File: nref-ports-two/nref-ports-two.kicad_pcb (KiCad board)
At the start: 2 copper layers, 88 x 24.9 mm, 6 parts, among them J1 USB_C_Receptacle, J2 USB_C_Receptacle, J3 WURTH_692121230100, J4 HD0919MSMTTR

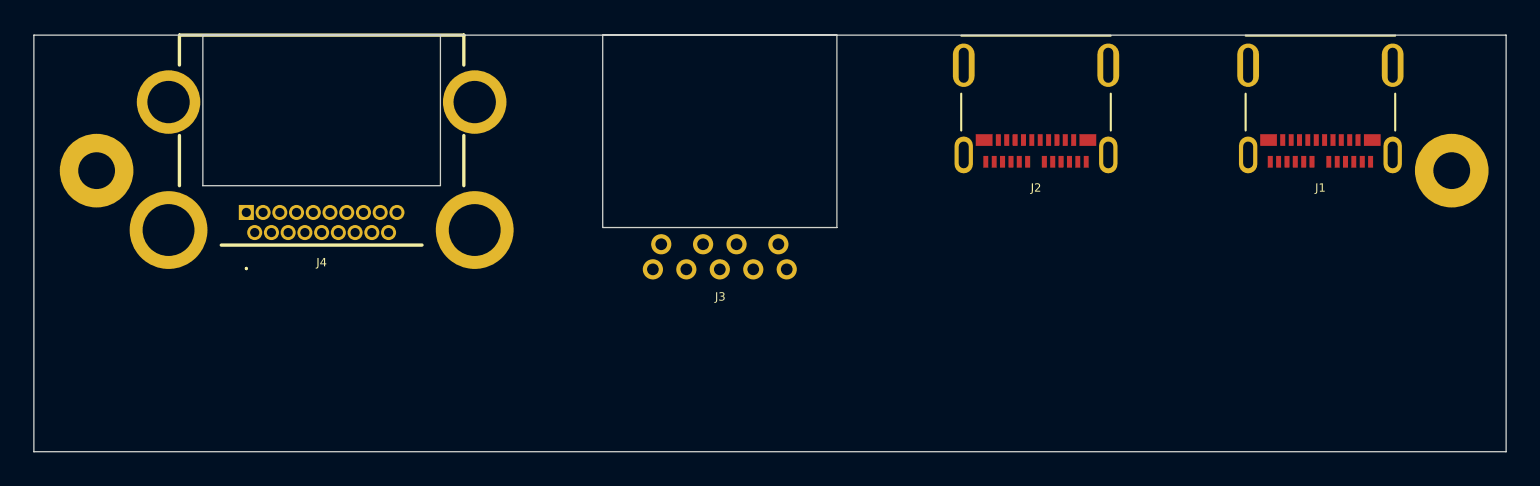
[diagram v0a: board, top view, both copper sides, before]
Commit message: ports 1 routing, ports 2 location tweaks
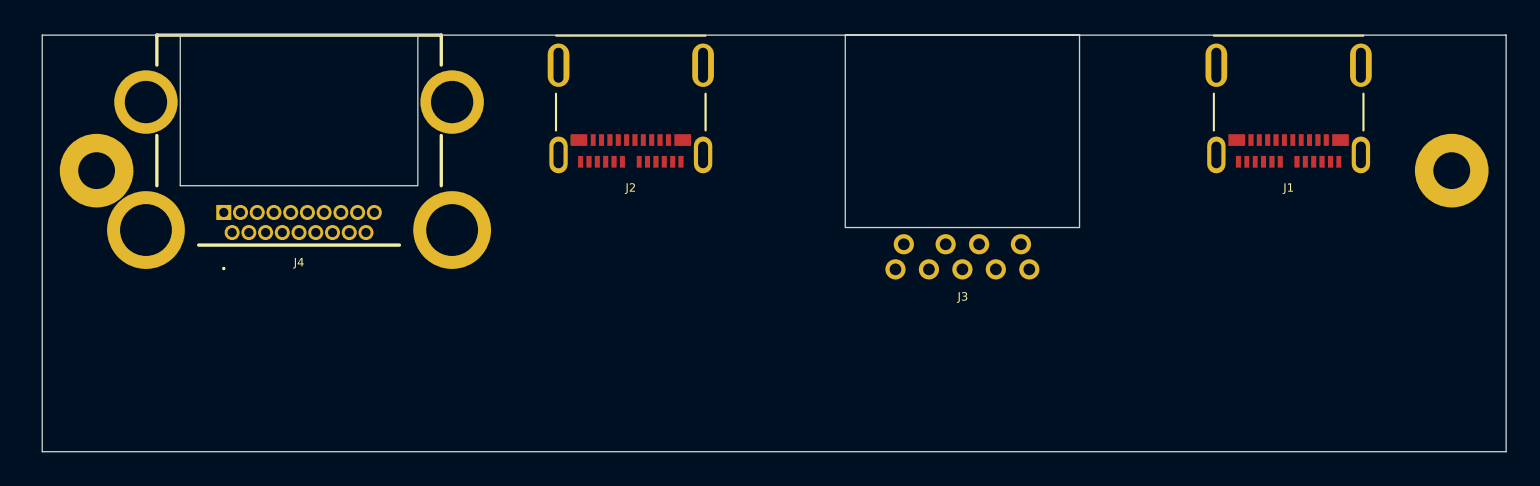
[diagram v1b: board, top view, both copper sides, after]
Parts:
- moved J2 24.2 mm to (135.7, 83.8)
- moved J3 14.5 mm to (155.5, 94.0)
- moved J1 1.90 mm to (175.0, 83.8)
- moved J4 1.35 mm to (111.3, 90.6)
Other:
- board size 88 x 24.9 mm -> 87.5 x 24.9 mm
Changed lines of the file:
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@@
 				(font
 					(size 1.27 1.27)
+					(thickness 0.15)
 				)
 			)
@@
 				(font
 					(size 1.27 1.27)
+					(thickness 0.15)
 				)
 			)
@@
 				(font
 					(size 1.27 1.27)
+					(thickness 0.15)
 				)
 			)
@@
 				(font
 					(size 1.27 1.27)
+					(thickness 0.15)
 				)
 			)
@@
 				(font
 					(size 1.27 1.27)
+					(thickness 0.15)
 				)
 			)
@@
 				(font
 					(size 1.27 1.27)
+					(thickness 0.15)
 				)
 			)
@@
 	(footprint "footprints:HD0919MSMTTR"
 		(layer "F.Cu")
-		(at 112.7 90.6)
+		(at 111.35 90.6)
 		(descr "HD09-19-MSMT-TR-3")
 		(tags "Connector")
@@
 				(font
 					(size 1.27 1.27)
+					(thickness 0.15)
 				)
 			)
@@
 				(font
 					(size 1.27 1.27)
+					(thickness 0.15)
 				)
 			)
@@
 				(font
 					(size 1.27 1.27)
+					(thickness 0.15)
 				)
 			)
@@
 	(footprint "footprints:WURTH_692121230100"
 		(layer "F.Cu")
-		(at 141 94 180)
+		(at 155.5 94 180)
 		(property "Reference" "J3"
 			(at -0.02855 -1.63745 0)
@@
 				(font
 					(size 1.27 1.27)
+					(thickness 0.15)
 				)
 			)
@@
 				(font
 					(size 1.27 1.27)
+					(thickness 0.15)
 				)
 			)
@@
 				(font
 					(size 1.27 1.27)
+					(thickness 0.15)
 				)
 			)
@@
 	(footprint "footprints:MOLEX_105450-0101"
 		(layer "F.Cu")
-		(at 159.9 83.8 180)
+		(at 135.68 83.8 180)
 		(property "Reference" "J2"
 			(at -0.000875 -5.327165 0)
@@
 				(font
 					(size 1.27 1.27)
+					(thickness 0.15)
 				)
 			)
@@
 				(font
 					(size 1.27 1.27)
+					(thickness 0.15)
 				)
 			)
@@
 				(font
 					(size 1.27 1.27)
+					(thickness 0.15)
 				)
 			)
@@
 			(polygon
 				(pts
-					(xy 163.40241 85.68) (xy 156.4 85.68) (xy 156.4 80.0274) (xy 163.40241 80.0274)
+					(xy 139.18241 85.68) (xy 132.18 85.68) (xy 132.18 80.0274) (xy 139.18241 80.0274)
 				)
 			)
@@
 	(footprint "footprints:MOLEX_105450-0101"
 		(layer "F.Cu")
-		(at 176.9 83.8 180)
+		(at 175 83.8 180)
 		(property "Reference" "J1"
 			(at -0.000875 -5.327165 0)
@@
 				(font
 					(size 1.27 1.27)
+					(thickness 0.15)
 				)
 			)
@@
 				(font
 					(size 1.27 1.27)
+					(thickness 0.15)
 				)
 			)
@@
 				(font
 					(size 1.27 1.27)
+					(thickness 0.15)
 				)
 			)
@@
 			(polygon
 				(pts
-					(xy 180.40241 85.68) (xy 173.4 85.68) (xy 173.4 80.0274) (xy 180.40241 80.0274)
+					(xy 178.50241 85.68) (xy 171.5 85.68) (xy 171.5 80.0274) (xy 178.50241 80.0274)
 				)
 			)
@@
 	)
 	(gr_rect
-		(start 100 80)
+		(start 100.5 80)
 		(end 188 104.9)
 		(stroke

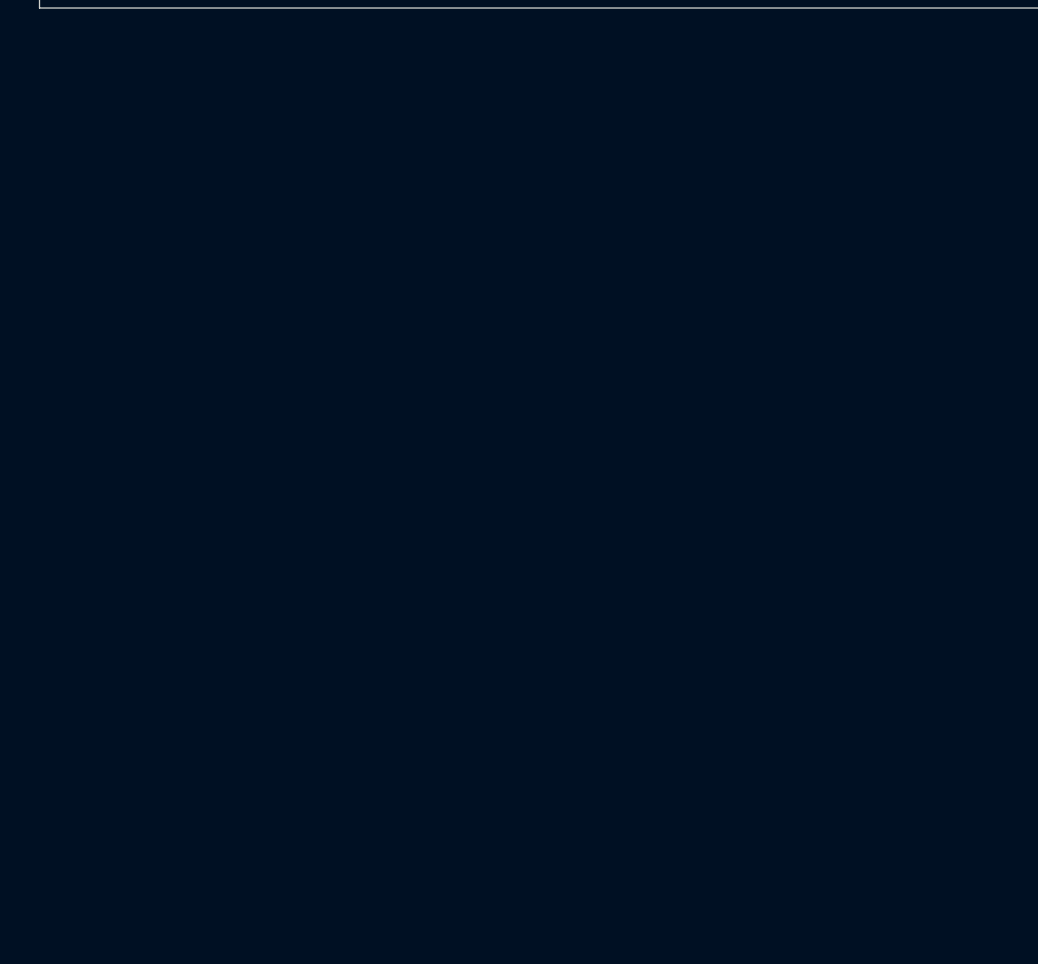
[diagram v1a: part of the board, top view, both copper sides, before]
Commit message: ports two: initial (mostly complete) schematic
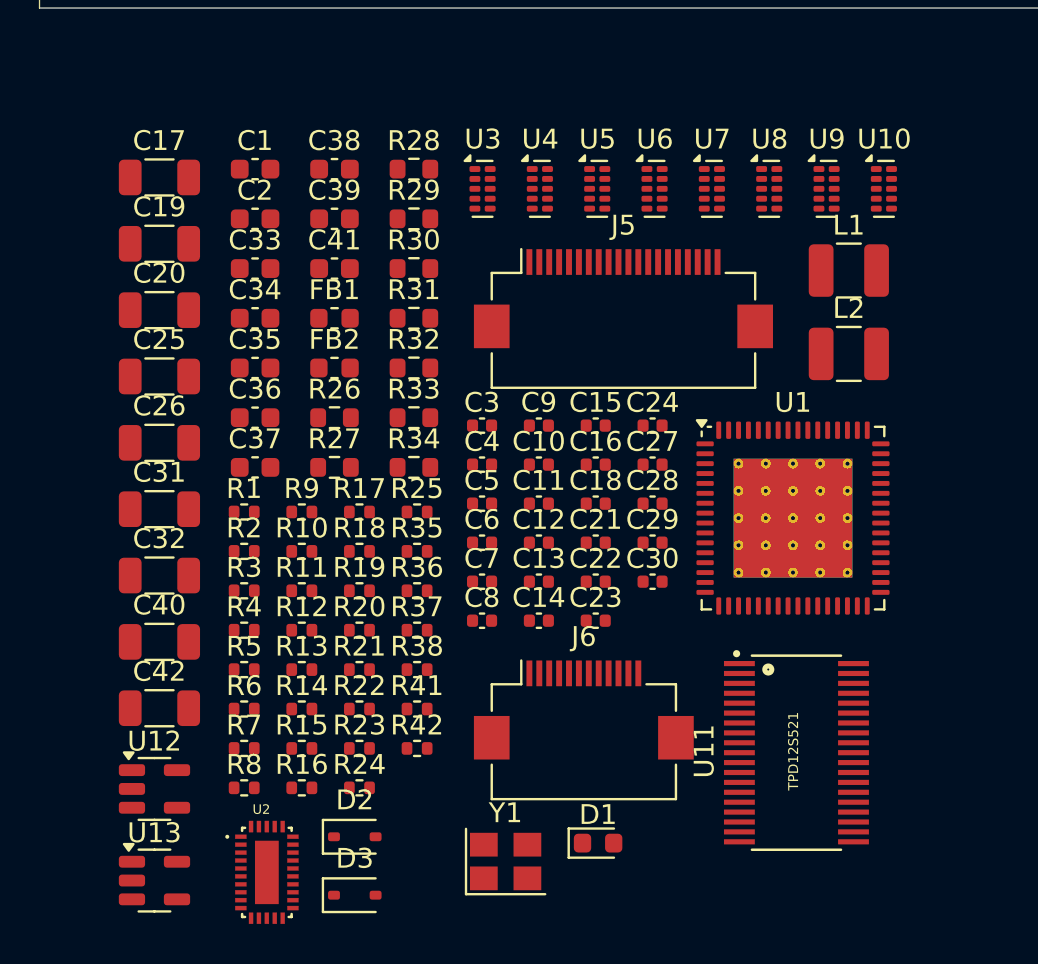
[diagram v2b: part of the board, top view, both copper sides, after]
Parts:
- added C1: 18pF, Capacitor_SMD:C_0603_1608Metric, F.Cu at (111.4, 113.0)
- added C10: 0.1uF, Capacitor_SMD:C_0402_1005Metric, F.Cu at (125.7, 128.0)
- added C11: 0.1uF, Capacitor_SMD:C_0402_1005Metric, F.Cu at (125.7, 129.9)
- added C12: 10uF, Capacitor_SMD:C_0402_1005Metric, F.Cu at (125.7, 131.9)
- added C13: 0.1uF, Capacitor_SMD:C_0402_1005Metric, F.Cu at (125.7, 133.9)
- added C14: 0.1uF, Capacitor_SMD:C_0402_1005Metric, F.Cu at (125.7, 135.8)
- added C15: 0.1uF, Capacitor_SMD:C_0402_1005Metric, F.Cu at (128.6, 126.0)
- added C16: 10uF, Capacitor_SMD:C_0402_1005Metric, F.Cu at (128.6, 128.0)
- added C17: 47uF, Capacitor_SMD:C_1206_3216Metric, F.Cu at (106.6, 113.5)
- added C18: 0.1uF, Capacitor_SMD:C_0402_1005Metric, F.Cu at (128.6, 129.9)
- added C19: 47uF, Capacitor_SMD:C_1206_3216Metric, F.Cu at (106.6, 116.8)
- added C2: 18pF, Capacitor_SMD:C_0603_1608Metric, F.Cu at (111.4, 115.5)
- added C20: 47uF, Capacitor_SMD:C_1206_3216Metric, F.Cu at (106.6, 120.2)
- added C21: 0.1uF, Capacitor_SMD:C_0402_1005Metric, F.Cu at (128.6, 131.9)
- added C22: 0.1uF, Capacitor_SMD:C_0402_1005Metric, F.Cu at (128.6, 133.9)
- added C23: 0.1uF, Capacitor_SMD:C_0402_1005Metric, F.Cu at (128.6, 135.8)
- added C24: 0.1uF, Capacitor_SMD:C_0402_1005Metric, F.Cu at (131.5, 126.0)
- added C25: 47uF, Capacitor_SMD:C_1206_3216Metric, F.Cu at (106.6, 123.5)
- added C26: 47uF, Capacitor_SMD:C_1206_3216Metric, F.Cu at (106.6, 126.9)
- added C27: 0.1uF, Capacitor_SMD:C_0402_1005Metric, F.Cu at (131.5, 128.0)
- added C28: 0.1uF, Capacitor_SMD:C_0402_1005Metric, F.Cu at (131.5, 129.9)
- added C29: 0.1uF, Capacitor_SMD:C_0402_1005Metric, F.Cu at (131.5, 131.9)
- added C3: 0.1uF, Capacitor_SMD:C_0402_1005Metric, F.Cu at (122.8, 126.0)
- added C30: 0.1uF, Capacitor_SMD:C_0402_1005Metric, F.Cu at (131.5, 133.9)
- added C31: 47uF, Capacitor_SMD:C_1206_3216Metric, F.Cu at (106.6, 130.2)
- added C32: 47uF, Capacitor_SMD:C_1206_3216Metric, F.Cu at (106.6, 133.6)
- added C33: 0.1uF, Capacitor_SMD:C_0603_1608Metric, F.Cu at (111.4, 118.1)
- added C34: 0.1uF, Capacitor_SMD:C_0603_1608Metric, F.Cu at (111.4, 120.6)
- added C35: 0.1uF, Capacitor_SMD:C_0603_1608Metric, F.Cu at (111.4, 123.1)
- added C36: 0.1uF, Capacitor_SMD:C_0603_1608Metric, F.Cu at (111.4, 125.6)
- added C37: 0.1uF, Capacitor_SMD:C_0603_1608Metric, F.Cu at (111.4, 128.1)
- added C38: 0.1uF, Capacitor_SMD:C_0603_1608Metric, F.Cu at (115.4, 113.0)
- added C39: 22uF, Capacitor_SMD:C_0603_1608Metric, F.Cu at (115.4, 115.5)
- added C4: 0.1uF, Capacitor_SMD:C_0402_1005Metric, F.Cu at (122.8, 128.0)
- added C40: 47uF, Capacitor_SMD:C_1206_3216Metric, F.Cu at (106.6, 136.9)
- added C41: 22uF, Capacitor_SMD:C_0603_1608Metric, F.Cu at (115.4, 118.1)
- added C42: 47uF, Capacitor_SMD:C_1206_3216Metric, F.Cu at (106.6, 140.3)
- added C5: 0.1uF, Capacitor_SMD:C_0402_1005Metric, F.Cu at (122.8, 129.9)
- added C6: 0.1uF, Capacitor_SMD:C_0402_1005Metric, F.Cu at (122.8, 131.9)
- added C7: 0.1uF, Capacitor_SMD:C_0402_1005Metric, F.Cu at (122.8, 133.9)
- added C8: 0.1uF, Capacitor_SMD:C_0402_1005Metric, F.Cu at (122.8, 135.8)
- added C9: 0.1uF, Capacitor_SMD:C_0402_1005Metric, F.Cu at (125.7, 126.0)
- added D1: SD0603S040S0R2, Diode_SMD:D_0603_1608Metric, F.Cu at (128.7, 147.1)
- added D2: PMEG1020EA,115, Diode_SMD:D_SOD-323, F.Cu at (116.4, 146.7)
- added D3: PMEG1020EA,115, Diode_SMD:D_SOD-323, F.Cu at (116.4, 149.7)
- added FB1: 220@100MHz 1.4A, Inductor_SMD:L_0603_1608Metric, F.Cu at (115.4, 120.6)
- added FB2: 220@100MHz 1.4A, Inductor_SMD:L_0603_1608Metric, F.Cu at (115.4, 123.1)
- added J5: Conn_01x20, Connector_FFC-FPC:Hirose_FH12-20S-0.5SH_1x20-1MP_P0.50mm_Horizontal, F.Cu at (130.0, 119.6)
- added J6: Conn_01x12_Pin, Connector_FFC-FPC:Hirose_FH12-12S-0.5SH_1x12-1MP_P0.50mm_Horizontal, F.Cu at (128.0, 140.3)
- added L1: 3.3uH, Inductor_SMD:L_1210_3225Metric, F.Cu at (141.4, 118.2)
- added L2: 2.2uH, Inductor_SMD:L_1210_3225Metric, F.Cu at (141.4, 122.4)
- added R1: 0, Resistor_SMD:R_0402_1005Metric, F.Cu at (110.8, 130.3)
- added R10: 0, Resistor_SMD:R_0402_1005Metric, F.Cu at (113.7, 132.3)
- added R11: 10k, Resistor_SMD:R_0402_1005Metric, F.Cu at (113.7, 134.3)
- added R12: 900k, Resistor_SMD:R_0402_1005Metric, F.Cu at (113.7, 136.3)
- added R13: 200k, Resistor_SMD:R_0402_1005Metric, F.Cu at (113.7, 138.3)
- added R14: 0, Resistor_SMD:R_0402_1005Metric, F.Cu at (113.7, 140.3)
- added R15: 0, Resistor_SMD:R_0402_1005Metric, F.Cu at (113.7, 142.3)
- added R16: 0, Resistor_SMD:R_0402_1005Metric, F.Cu at (113.7, 144.3)
- added R17: 0, Resistor_SMD:R_0402_1005Metric, F.Cu at (116.7, 130.3)
- added R18: 200k, Resistor_SMD:R_0402_1005Metric, F.Cu at (116.7, 132.3)
- added R19: 0, Resistor_SMD:R_0402_1005Metric, F.Cu at (116.7, 134.3)
- added R2: 1M, Resistor_SMD:R_0402_1005Metric, F.Cu at (110.8, 132.3)
- added R20: 0, Resistor_SMD:R_0402_1005Metric, F.Cu at (116.7, 136.3)
- added R21: 0, Resistor_SMD:R_0402_1005Metric, F.Cu at (116.7, 138.3)
- added R22: 200k, Resistor_SMD:R_0402_1005Metric, F.Cu at (116.7, 140.3)
- added R23: 200k, Resistor_SMD:R_0402_1005Metric, F.Cu at (116.7, 142.3)
- added R24: 200k, Resistor_SMD:R_0402_1005Metric, F.Cu at (116.7, 144.3)
- added R25: 0, Resistor_SMD:R_0402_1005Metric, F.Cu at (119.6, 130.3)
- added R26: 10k, Resistor_SMD:R_0603_1608Metric, F.Cu at (115.4, 125.6)
- added R27: 4.7k, Resistor_SMD:R_0603_1608Metric, F.Cu at (115.4, 128.1)
- added R28: 27k, Resistor_SMD:R_0603_1608Metric, F.Cu at (119.4, 113.0)
- added R29: 4.7k, Resistor_SMD:R_0603_1608Metric, F.Cu at (119.4, 115.5)
- added R3: 100k, Resistor_SMD:R_0402_1005Metric, F.Cu at (110.8, 134.3)
- added R30: 10k, Resistor_SMD:R_0603_1608Metric, F.Cu at (119.4, 118.1)
- added R31: 100k, Resistor_SMD:R_0603_1608Metric, F.Cu at (119.4, 120.6)
- added R32: 47k, Resistor_SMD:R_0603_1608Metric, F.Cu at (119.4, 123.1)
- added R33: 47k, Resistor_SMD:R_0603_1608Metric, F.Cu at (119.4, 125.6)
- added R34: 47k, Resistor_SMD:R_0603_1608Metric, F.Cu at (119.4, 128.1)
- added R35: 100k, Resistor_SMD:R_0402_1005Metric, F.Cu at (119.6, 132.3)
- added R36: 100k, Resistor_SMD:R_0402_1005Metric, F.Cu at (119.6, 134.3)
- added R37: 8.25k, Resistor_SMD:R_0402_1005Metric, F.Cu at (119.6, 136.3)
- added R38: 10k, Resistor_SMD:R_0402_1005Metric, F.Cu at (119.6, 138.3)
- added R4: 90.9K 1%, Resistor_SMD:R_0402_1005Metric, F.Cu at (110.8, 136.3)
- added R41: 45.3k, Resistor_SMD:R_0402_1005Metric, F.Cu at (119.6, 140.3)
- added R42: 10k, Resistor_SMD:R_0402_1005Metric, F.Cu at (119.6, 142.3)
- added R5: 4.7k, Resistor_SMD:R_0402_1005Metric, F.Cu at (110.8, 138.3)
- added R6: 10k, Resistor_SMD:R_0402_1005Metric, F.Cu at (110.8, 140.3)
- added R7: 9.53K 1%, Resistor_SMD:R_0402_1005Metric, F.Cu at (110.8, 142.3)
- added R8: 4.7k, Resistor_SMD:R_0402_1005Metric, F.Cu at (110.8, 144.3)
- added R9: 4.7k, Resistor_SMD:R_0402_1005Metric, F.Cu at (113.7, 130.3)
- added U1: TUSB8041, Package_DFN_QFN:QFN-64-1EP_9x9mm_P0.5mm_EP6x6mm_ThermalVias, F.Cu at (138.5, 130.7)
- added U10: TPD4E02B04DQA, Package_SON:USON-10_2.5x1.0mm_P0.5mm, F.Cu at (143.1, 114.0)
- added U11: TPD12S521, footprints:TSSOP50P640X120-38N, F.Cu at (138.7, 142.5)
- added U12: LM2830XQMFE/NOPB, Package_TO_SOT_SMD:SOT-23-5, F.Cu at (106.3, 144.3)
- added U13: LM2830XQMFE/NOPB, Package_TO_SOT_SMD:SOT-23-5, F.Cu at (106.3, 149.0)
- added U2: HD3SS3220IRNHT, footprints:QFN40P450X250X80-31N120X320, F.Cu at (112.0, 148.5)
- added U3: TPD4E02B04DQA, Package_SON:USON-10_2.5x1.0mm_P0.5mm, F.Cu at (122.9, 114.0)
- added U4: TPD4E02B04DQA, Package_SON:USON-10_2.5x1.0mm_P0.5mm, F.Cu at (125.8, 114.0)
- added U5: TPD4E02B04DQA, Package_SON:USON-10_2.5x1.0mm_P0.5mm, F.Cu at (128.7, 114.0)
- added U6: TPD4E02B04DQA, Package_SON:USON-10_2.5x1.0mm_P0.5mm, F.Cu at (131.6, 114.0)
- added U7: TPD4E02B04DQA, Package_SON:USON-10_2.5x1.0mm_P0.5mm, F.Cu at (134.4, 114.0)
- added U8: TPD4E02B04DQA, Package_SON:USON-10_2.5x1.0mm_P0.5mm, F.Cu at (137.3, 114.0)
- added U9: TPD4E02B04DQA, Package_SON:USON-10_2.5x1.0mm_P0.5mm, F.Cu at (140.2, 114.0)
- added Y1: 24MHz, Crystal:Crystal_SMD_Abracon_ABM8G-4Pin_3.2x2.5mm, F.Cu at (124.0, 148.0)
- J3: value WURTH_692121230100 -> USB3_A
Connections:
- J1 pad A1: (no net) -> GND
- J1 pad A10: (no net) -> USBH_2B_RXN
- J1 pad A11: (no net) -> USBH_2B_RXP
- J1 pad A12: (no net) -> GND
- J1 pad A2: (no net) -> /USBH_2A_AC_TXP
- J1 pad A3: (no net) -> /USBH_2A_AC_TXN
- J1 pad A4: (no net) -> +5V
- J1 pad A5: (no net) -> CC1
- J1 pad A6: (no net) -> USBH_2_DP
- J1 pad A7: (no net) -> USBH_2_DN
- J1 pad A8: (no net) -> unconnected-(J1-SBU1-PadA8)
- J1 pad A9: (no net) -> +5V
- J1 pad B1: (no net) -> GND
- J1 pad B10: (no net) -> USBH_2A_RXN
- J1 pad B11: (no net) -> USBH_2A_RXP
- J1 pad B12: (no net) -> GND
- J1 pad B2: (no net) -> /USBH_2B_AC_TXP
- J1 pad B3: (no net) -> /USBH_2B_AC_TXN
- J1 pad B4: (no net) -> +5V
- J1 pad B5: (no net) -> CC2
- J1 pad B6: (no net) -> USBH_2_DP
- J1 pad B7: (no net) -> USBH_2_DN
- J1 pad B8: (no net) -> unconnected-(J1-SBU2-PadB8)
- J1 pad B9: (no net) -> +5V
- J1 pad S1: (no net) -> GND
- J2 pad A1: (no net) -> GND
- J2 pad A10: (no net) -> USBH_MUXB_RXN
- J2 pad A11: (no net) -> USBH_MUXB_RXP
- J2 pad A12: (no net) -> GND
- J2 pad A2: (no net) -> /USBH_1A_AC_TXP
- J2 pad A3: (no net) -> /USBH_1A_AC_TXN
- J2 pad A4: (no net) -> +5V
- J2 pad A5: (no net) -> Net-(J2-CC1)
- J2 pad A6: (no net) -> USBH_1_DP
- J2 pad A7: (no net) -> USBH_1_DN
- J2 pad A8: (no net) -> unconnected-(J2-SBU1-PadA8)
- J2 pad A9: (no net) -> +5V
- J2 pad B1: (no net) -> GND
- J2 pad B10: (no net) -> USBH_MUXA_RXN
- J2 pad B11: (no net) -> USBH_MUXA_RXP
- J2 pad B12: (no net) -> GND
- J2 pad B2: (no net) -> /USBH_1B_AC_TXP
- J2 pad B3: (no net) -> /USBH_1B_AC_TXN
- J2 pad B4: (no net) -> +5V
- J2 pad B5: (no net) -> Net-(J2-CC2)
- J2 pad B6: (no net) -> USBH_1_DP
- J2 pad B7: (no net) -> USBH_1_DN
- J2 pad B8: (no net) -> unconnected-(J2-SBU2-PadB8)
- J2 pad B9: (no net) -> +5V
- J2 pad S1: (no net) -> GND
- J3 pad 1: (no net) -> +5V
- J3 pad 2: (no net) -> USBH_3_DN
- J3 pad 3: (no net) -> USBH_3_DP
- J3 pad 4: (no net) -> GND
- J3 pad 5: (no net) -> USBH_1A_RXN
- J3 pad 6: (no net) -> USBH_1A_RXP
- J3 pad 7: (no net) -> GND
- J3 pad 8: (no net) -> /USB3_1_SSTXCN
- J3 pad 9: (no net) -> /USB3_1_SSTXCP
- J4 pad 1: (no net) -> HDMI_TX2P
- J4 pad 10: (no net) -> HDMI_CLKP
- J4 pad 11: (no net) -> GND
- J4 pad 12: (no net) -> HDMI_CLKN
- J4 pad 13: (no net) -> Net-(J4-CEC)
- J4 pad 14: (no net) -> unconnected-(J4-UTILITY-Pad14)
- J4 pad 15: (no net) -> Net-(J4-SCL)
- J4 pad 16: (no net) -> Net-(J4-SDA)
- J4 pad 17: (no net) -> GND
- J4 pad 18: (no net) -> Net-(J4-+5V)
- J4 pad 19: (no net) -> Net-(J4-HPD)
- J4 pad 2: (no net) -> GND
- J4 pad 3: (no net) -> HDMI_TX2N
- J4 pad 4: (no net) -> HDMI_TX1P
- J4 pad 5: (no net) -> GND
- J4 pad 6: (no net) -> HDMI_TX1N
- J4 pad 7: (no net) -> HDMI_TX0P
- J4 pad 8: (no net) -> GND
- J4 pad 9: (no net) -> HDMI_TX0N

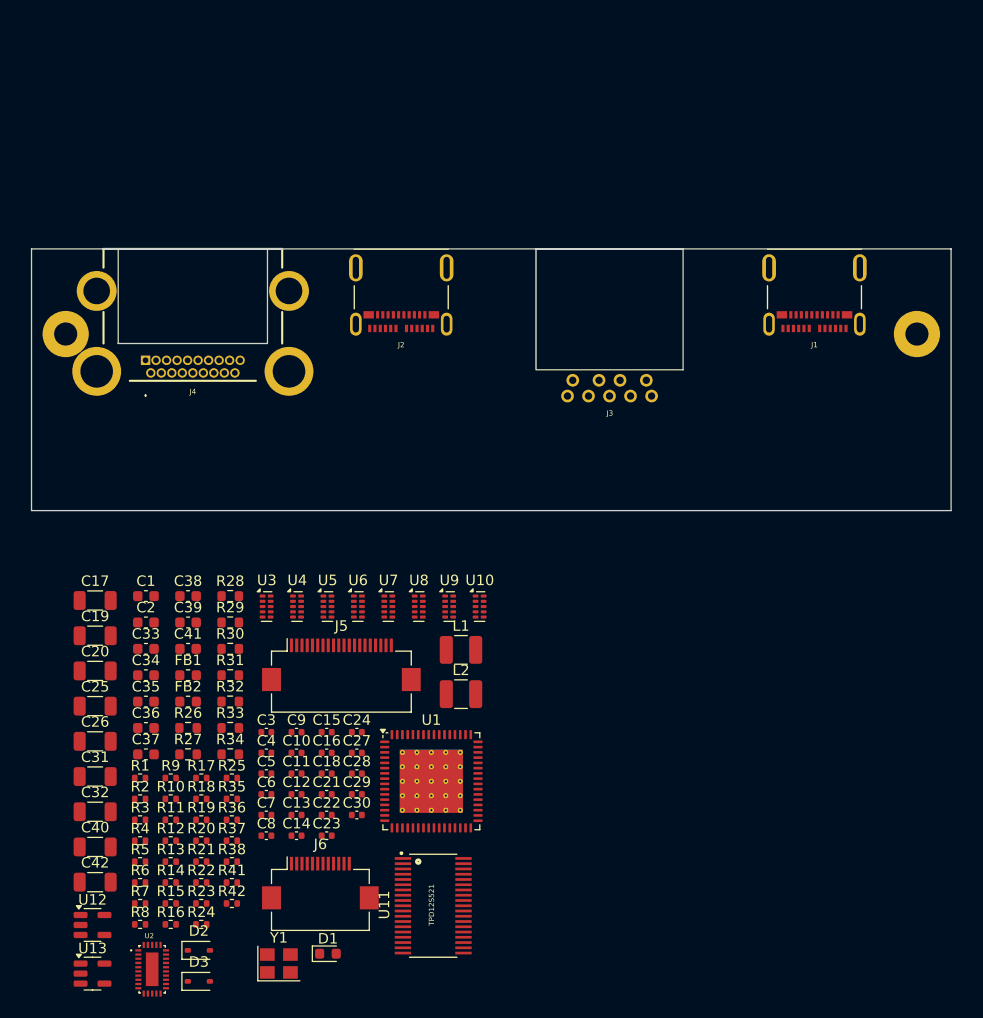
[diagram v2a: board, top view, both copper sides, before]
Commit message: ports two: rough placement of components
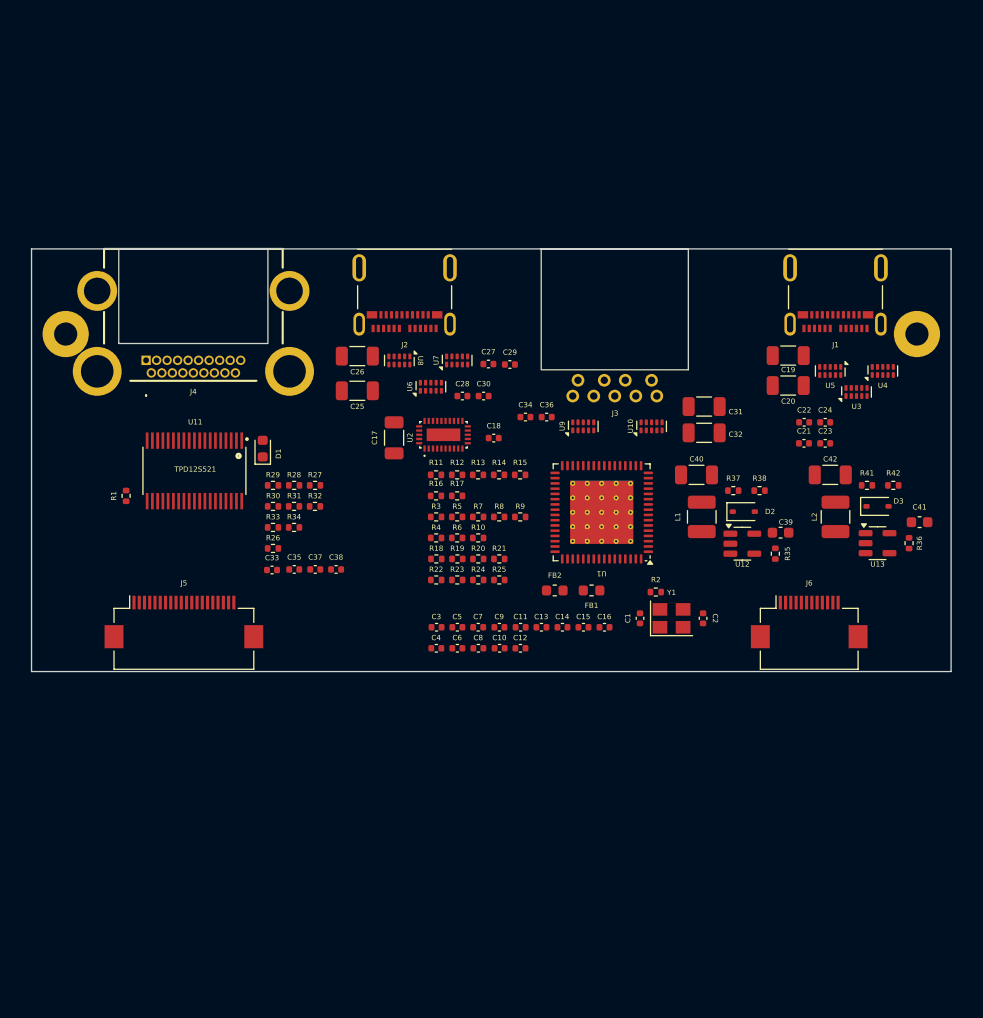
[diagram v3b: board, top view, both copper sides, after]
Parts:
- C1, C2, C33, C34, C35, C36, C37, C38: footprint Capacitor_SMD:C_0603_1608Metric -> Capacitor_SMD:C_0402_1005Metric
- R26, R27, R28, R29, R30, R31, R32, R33, R34: footprint Resistor_SMD:R_0603_1608Metric -> Resistor_SMD:R_0402_1005Metric
- moved U13 85.2 mm to (181.0, 108.0)
- moved C42 80.0 mm to (176.5, 101.5), turned to 180 degrees
- moved D3 78.8 mm to (181.0, 104.5)
- moved R42 74.5 mm to (182.5, 102.5)
- moved U12 71.7 mm to (168.1, 108.0)
- moved C20 71.3 mm to (172.5, 93.0), turned to 180 degrees
- moved R41 71.3 mm to (180.0, 102.5)
- moved C19 71.1 mm to (172.5, 90.2), turned to 180 degrees
- moved C41 70.6 mm to (185.0, 106.0)
- moved R36 69.6 mm to (184.0, 108.0), turned to -90 degrees
- moved C32 68.2 mm to (164.5, 97.5)
- moved C31 67.8 mm to (164.5, 95.0)
- moved C40 67.3 mm to (163.8, 101.5), turned to 180 degrees
- moved D2 66.6 mm to (168.3, 105.0)
- moved R38 61.4 mm to (169.8, 103.0)
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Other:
- board size 87.5 x 24.9 mm -> 87.5 x 40.2 mm
